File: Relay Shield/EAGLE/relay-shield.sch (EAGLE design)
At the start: 45 parts, among them J1 POWER_JACKSLT, Q1 MPSA42, Q2 MPSA42, Q3 MPSA42, Q4 MPSA42, U1 RELAYPANASONIC-JS, U2 RELAYPANASONIC-JS, U3 RELAYPANASONIC-JS, U4 RELAYPANASONIC-JS, U5 SPARK_CORE, U6 AP1509-50SG-13

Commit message: updated relay shield gerbers to v201
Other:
- note added: "v2.0.1"
- note removed: "v2.0"
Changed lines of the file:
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@@
 <?xml version="1.0" encoding="utf-8"?>
 <!DOCTYPE eagle SYSTEM "eagle.dtd">
-<eagle version="6.3">
+<eagle version="6.5.0">
 <drawing>
 <settings>
@@
 <setting verticaltext="up"/>
 </settings>
-<grid distance="0.1" unitdist="inch" unit="inch" style="lines" multiple="1" display="yes" altdistance="0.01" altunitdist="inch" altunit="inch"/>
+<grid distance="0.1" unitdist="inch" unit="inch" style="lines" multiple="1" display="no" altdistance="0.01" altunitdist="inch" altunit="inch"/>
 <layers>
-<layer number="1" name="Top" color="4" fill="1" visible="no" active="no"/>
-<layer number="2" name="Route2" color="1" fill="3" visible="no" active="no"/>
-<layer number="3" name="Route3" color="4" fill="3" visible="no" active="no"/>
-<layer number="4" name="Route4" color="1" fill="4" visible="no" active="no"/>
-<layer number="5" name="Route5" color="4" fill="4" visible="no" active="no"/>
-<layer number="6" name="Route6" color="1" fill="8" visible="no" active="no"/>
-<layer number="7" name="Route7" color="4" fill="8" visible="no" active="no"/>
-<layer number="8" name="Route8" color="1" fill="2" visible="no" active="no"/>
-<layer number="9" name="Route9" color="4" fill="2" visible="no" active="no"/>
-<layer number="10" name="Route10" color="1" fill="7" visible="no" active="no"/>
-<layer number="11" name="Route11" color="4" fill="7" visible="no" active="no"/>
-<layer number="12" name="Route12" color="1" fill="5" visible="no" active="no"/>
-<layer number="13" name="Route13" color="4" fill="5" visible="no" active="no"/>
-<layer number="14" name="Route14" color="1" fill="6" visible="no" active="no"/>
-<layer number="15" name="Route15" color="4" fill="6" visible="no" active="no"/>
-<layer number="16" name="Bottom" color="1" fill="1" visible="no" active="no"/>
-<layer number="17" name="Pads" color="2" fill="1" visible="no" active="no"/>
-<layer number="18" name="Vias" color="2" fill="1" visible="no" active="no"/>
-<layer number="19" name="Unrouted" color="6" fill="1" visible="no" active="no"/>
-<layer number="20" name="Dimension" color="15" fill="1" visible="no" active="no"/>
-<layer number="21" name="tPlace" color="16" fill="1" visible="no" active="no"/>
-<layer number="22" name="bPlace" color="14" fill="1" visible="no" active="no"/>
-<layer number="23" name="tOrigins" color="15" fill="1" visible="no" active="no"/>
-<layer number="24" name="bOrigins" color="15" fill="1" visible="no" active="no"/>
-<layer number="25" name="tNames" color="7" fill="1" visible="no" active="no"/>
-<layer number="26" name="bNames" color="7" fill="1" visible="no" active="no"/>
-<layer number="27" name="tValues" color="7" fill="1" visible="no" active="no"/>
-<layer number="28" name="bValues" color="7" fill="1" visible="no" active="no"/>
+<layer number="1" name="Top" color="4" fill="1" visible="yes" active="no"/>
+<layer number="2" name="Route2" color="1" fill="3" visible="yes" active="no"/>
+<layer number="3" name="Route3" color="4" fill="3" visible="yes" active="no"/>
+<layer number="4" name="Route4" color="1" fill="4" visible="yes" active="no"/>
+<layer number="5" name="Route5" color="4" fill="4" visible="yes" active="no"/>
+<layer number="6" name="Route6" color="1" fill="8" visible="yes" active="no"/>
+<layer number="7" name="Route7" color="4" fill="8" visible="yes" active="no"/>
+<layer number="8" name="Route8" color="1" fill="2" visible="yes" active="no"/>
+<layer number="9" name="Route9" color="4" fill="2" visible="yes" active="no"/>
+<layer number="10" name="Route10" color="1" fill="7" visible="yes" active="no"/>
+<layer number="11" name="Route11" color="4" fill="7" visible="yes" active="no"/>
+<layer number="12" name="Route12" color="1" fill="5" visible="yes" active="no"/>
+<layer number="13" name="Route13" color="4" fill="5" visible="yes" active="no"/>
+<layer number="14" name="Route14" color="1" fill="6" visible="yes" active="no"/>
+<layer number="15" name="Route15" color="4" fill="6" visible="yes" active="no"/>
+<layer number="16" name="Bottom" color="1" fill="1" visible="yes" active="no"/>
+<layer number="17" name="Pads" color="2" fill="1" visible="yes" active="no"/>
+<layer number="18" name="Vias" color="2" fill="1" visible="yes" active="no"/>
+<layer number="19" name="Unrouted" color="6" fill="1" visible="yes" active="no"/>
+<layer number="20" name="Dimension" color="15" fill="1" visible="yes" active="no"/>
+<layer number="21" name="tPlace" color="16" fill="1" visible="yes" active="no"/>
+<layer number="22" name="bPlace" color="14" fill="1" visible="yes" active="no"/>
+<layer number="23" name="tOrigins" color="15" fill="1" visible="yes" active="no"/>
+<layer number="24" name="bOrigins" color="15" fill="1" visible="yes" active="no"/>
+<layer number="25" name="tNames" color="7" fill="1" visible="yes" active="no"/>
+<layer number="26" name="bNames" color="7" fill="1" visible="yes" active="no"/>
+<layer number="27" name="tValues" color="7" fill="1" visible="yes" active="no"/>
+<layer number="28" name="bValues" color="7" fill="1" visible="yes" active="no"/>
 <layer number="29" name="tStop" color="7" fill="3" visible="no" active="no"/>
 <layer number="30" name="bStop" color="7" fill="6" visible="no" active="no"/>
@@
 <layer number="35" name="tGlue" color="7" fill="4" visible="no" active="no"/>
 <layer number="36" name="bGlue" color="7" fill="5" visible="no" active="no"/>
-<layer number="37" name="tTest" color="7" fill="1" visible="no" active="no"/>
-<layer number="38" name="bTest" color="7" fill="1" visible="no" active="no"/>
+<layer number="37" name="tTest" color="7" fill="1" visible="yes" active="no"/>
+<layer number="38" name="bTest" color="7" fill="1" visible="yes" active="no"/>
 <layer number="39" name="tKeepout" color="4" fill="11" visible="no" active="no"/>
 <layer number="40" name="bKeepout" color="1" fill="11" visible="no" active="no"/>
@@
 <layer number="44" name="Drills" color="7" fill="1" visible="no" active="no"/>
 <layer number="45" name="Holes" color="7" fill="1" visible="no" active="no"/>
-<layer number="46" name="Milling" color="3" fill="1" visible="no" active="no"/>
-<layer number="47" name="Measures" color="7" fill="1" visible="no" active="no"/>
-<layer number="48" name="Document" color="7" fill="1" visible="no" active="no"/>
-<layer number="49" name="Reference" color="7" fill="1" visible="no" active="no"/>
-<layer number="50" name="dxf" color="7" fill="1" visible="no" active="no"/>
-<layer number="51" name="tDocu" color="6" fill="1" visible="no" active="no"/>
-<layer number="52" name="bDocu" color="7" fill="1" visible="no" active="no"/>
-<layer number="53" name="tGND_GNDA" color="7" fill="9" visible="no" active="no"/>
-<layer number="54" name="bGND_GNDA" color="1" fill="9" visible="no" active="no"/>
-<layer number="56" name="wert" color="7" fill="1" visible="no" active="no"/>
-<layer number="57" name="tCAD" color="7" fill="1" visible="no" active="no"/>
-<layer number="59" name="tCarbon" color="7" fill="1" visible="no" active="no"/>
-<layer number="60" name="bCarbon" color="7" fill="1" visible="no" active="no"/>
+<layer number="46" name="Milling" color="3" fill="1" visible="yes" active="no"/>
+<layer number="47" name="Measures" color="7" fill="1" visible="yes" active="no"/>
+<layer number="48" name="Document" color="7" fill="1" visible="yes" active="no"/>
+<layer number="49" name="Reference" color="7" fill="1" visible="yes" active="no"/>
+<layer number="50" name="dxf" color="7" fill="1" visible="yes" active="no"/>
+<layer number="51" name="tDocu" color="6" fill="1" visible="yes" active="no"/>
+<layer number="52" name="bDocu" color="7" fill="1" visible="yes" active="no"/>
+<layer number="53" name="tGND_GNDA" color="7" fill="9" visible="yes" active="no"/>
+<layer number="54" name="bGND_GNDA" color="1" fill="9" visible="yes" active="no"/>
+<layer number="56" name="wert" color="7" fill="1" visible="yes" active="no"/>
+<layer number="57" name="tCAD" color="7" fill="1" visible="yes" active="no"/>
+<layer number="59" name="tCarbon" color="7" fill="1" visible="yes" active="no"/>
+<layer number="60" name="bCarbon" color="7" fill="1" visible="yes" active="no"/>
 <layer number="91" name="Nets" color="2" fill="1" visible="yes" active="yes"/>
 <layer number="92" name="Busses" color="1" fill="1" visible="yes" active="yes"/>
@@
 <text x="2.54" y="5.08" size="3.81" layer="94">Relay Shield design by Spark Devices
 Libraries by Sparkfun</text>
-<text x="237.49" y="6.35" size="2.54" layer="94">v2.0</text>
+<text x="236.22" y="6.35" size="2.54" layer="94">v2.0.1</text>
 <text x="259.08" y="5.08" size="1.778" layer="95">Reference Designs ARE PROVIDED "AS IS" AND "WITH ALL FAULTS. SPARK LABS, INC
 ("SPARK") DISCLAIMS ALL OTHER WARRANTIES, EXPRESS OR IMPLIED, REGARDING

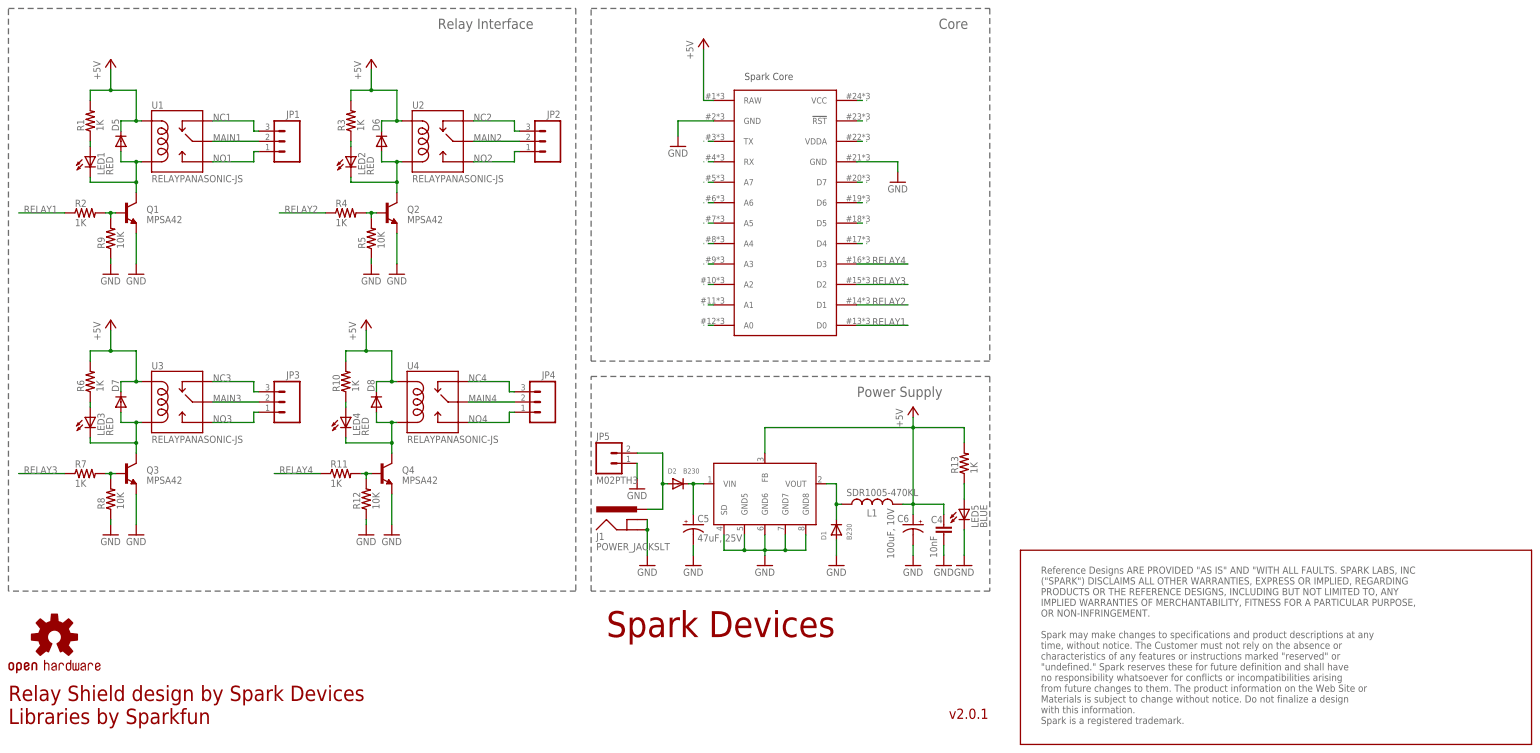
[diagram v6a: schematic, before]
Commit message: updated relay shield files to v210
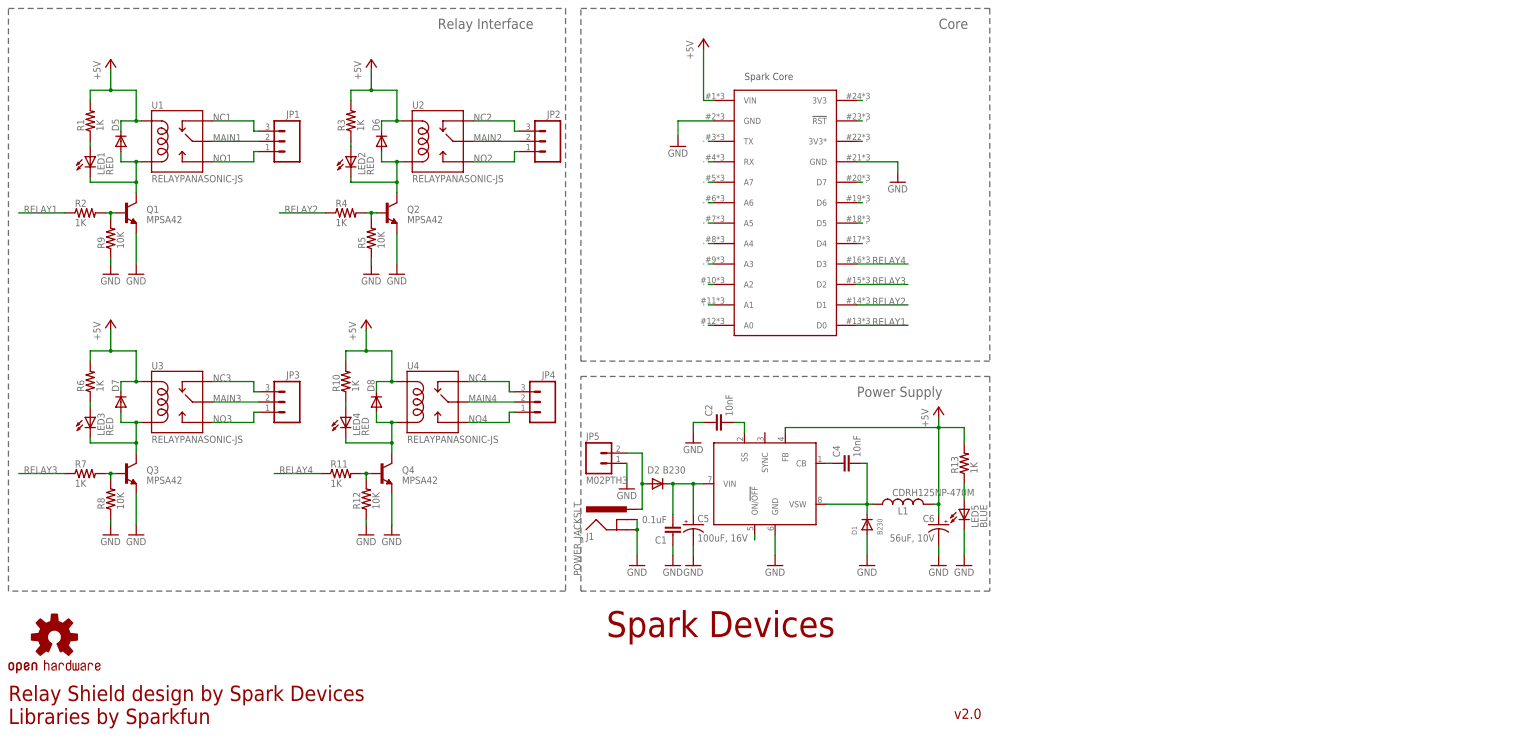
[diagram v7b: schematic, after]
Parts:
- removed U6: AP1509-50SG-13, Spark:AP1509-50SG-13
- added C1: 0.1uF, SparkFun-Capacitors:0.1UF-25V-5%(0603)
- added C2: 10nF, SparkFun-Capacitors:CAP0603-CAP
- added U$2: LM2672, Spark:LM2672
- C5: value 47uF, 25V -> 100uF, 16V
- C6: value 100uF, 10V -> 56uF, 10V
- L1: value SDR1005-470KL -> CDRH125NP-470M; device Spark:INDUCTOR-SPARKFUN -> SparkFun-Passives:INDUCTORPWR
- renumbered U5 to U$1
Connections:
- new net N$33: C4.1, U$2.CB
- new net N$35: U$2.ON/!OFF
- new net N$36: C2.2, U$2.SS
- net +5V: now also U$1.VIN, U$2.FB; no longer C4.2, U$1.RAW, U6.FB
- net GND: now also C1.1, C2.1, U$2.GND; no longer C4.1, U6.GND5, U6.GND6, U6.GND7, U6.GND8, U6.SD
- net N$14: now also C1.2, U$2.VIN; no longer U6.VIN
- net N$19: now also U$1.3V3*; no longer U$1.VDDA
- net N$21: now also U$1.3V3; no longer U$1.VCC
- net N$34: now also C4.2, U$2.VSW; no longer U6.VOUT
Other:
- note added: "v2.0"
- note removed: "Reference Designs ARE PROVIDED "AS IS" AND "WITH ALL FAULTS. SPARK LABS, INC ("SPARK") DISCLAIMS ALL OTHER WARRANTIES, EXPRESS OR IMPLIED, REGARDING PRODUCTS OR THE REFERENCE DESIGNS, INCLUDING BUT NOT LIMITED TO, ANY IMPLIED WARRANTIES OF MERCHANTABILITY, FITNESS FOR A PARTICULAR PURPOSE, OR NON-INFRINGEMENT. Spark may make changes to specifications and product descriptions at any time, without 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"
- note removed: "v2.0.1"
- moved on the sheet: C4, C6, D1, D2, J1, JP5, L1

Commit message: updated the bom and designator for regulator
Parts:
- renumbered U$2 to U6
